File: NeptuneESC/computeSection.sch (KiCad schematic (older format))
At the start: 15 parts, among them U1 ACS712xLCTR-20A, U2 ATmega8A-AU, Y1 16MHz

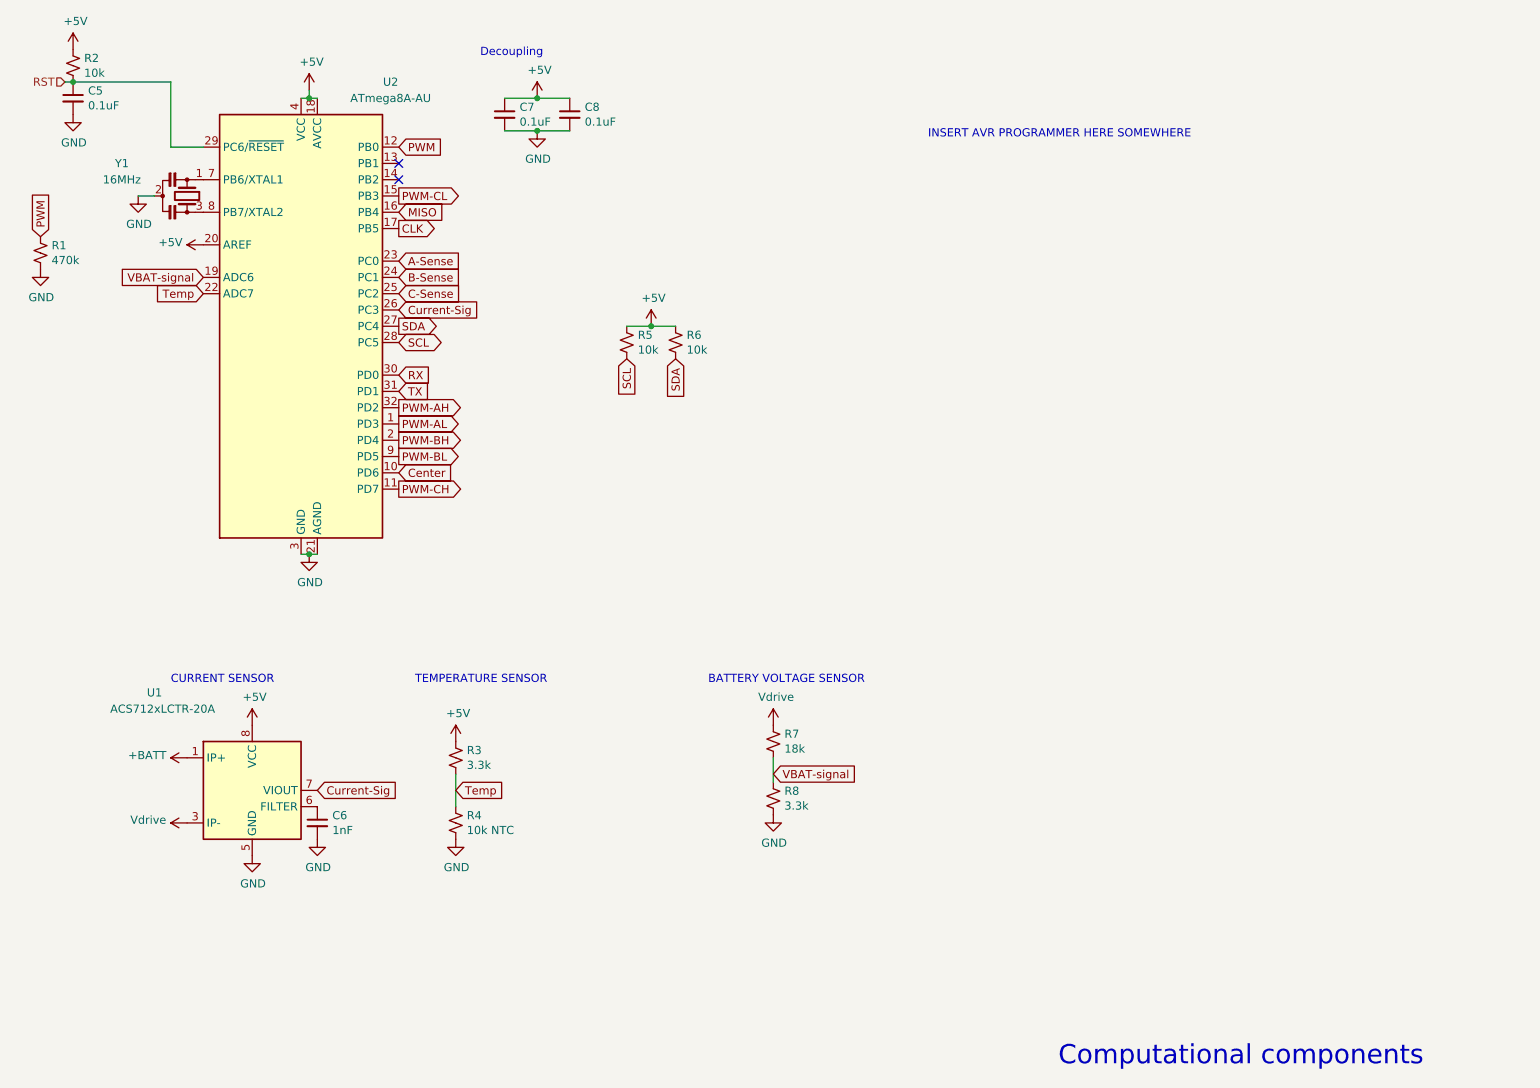
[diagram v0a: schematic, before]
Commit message: Innitial layout
Need to add motor pads
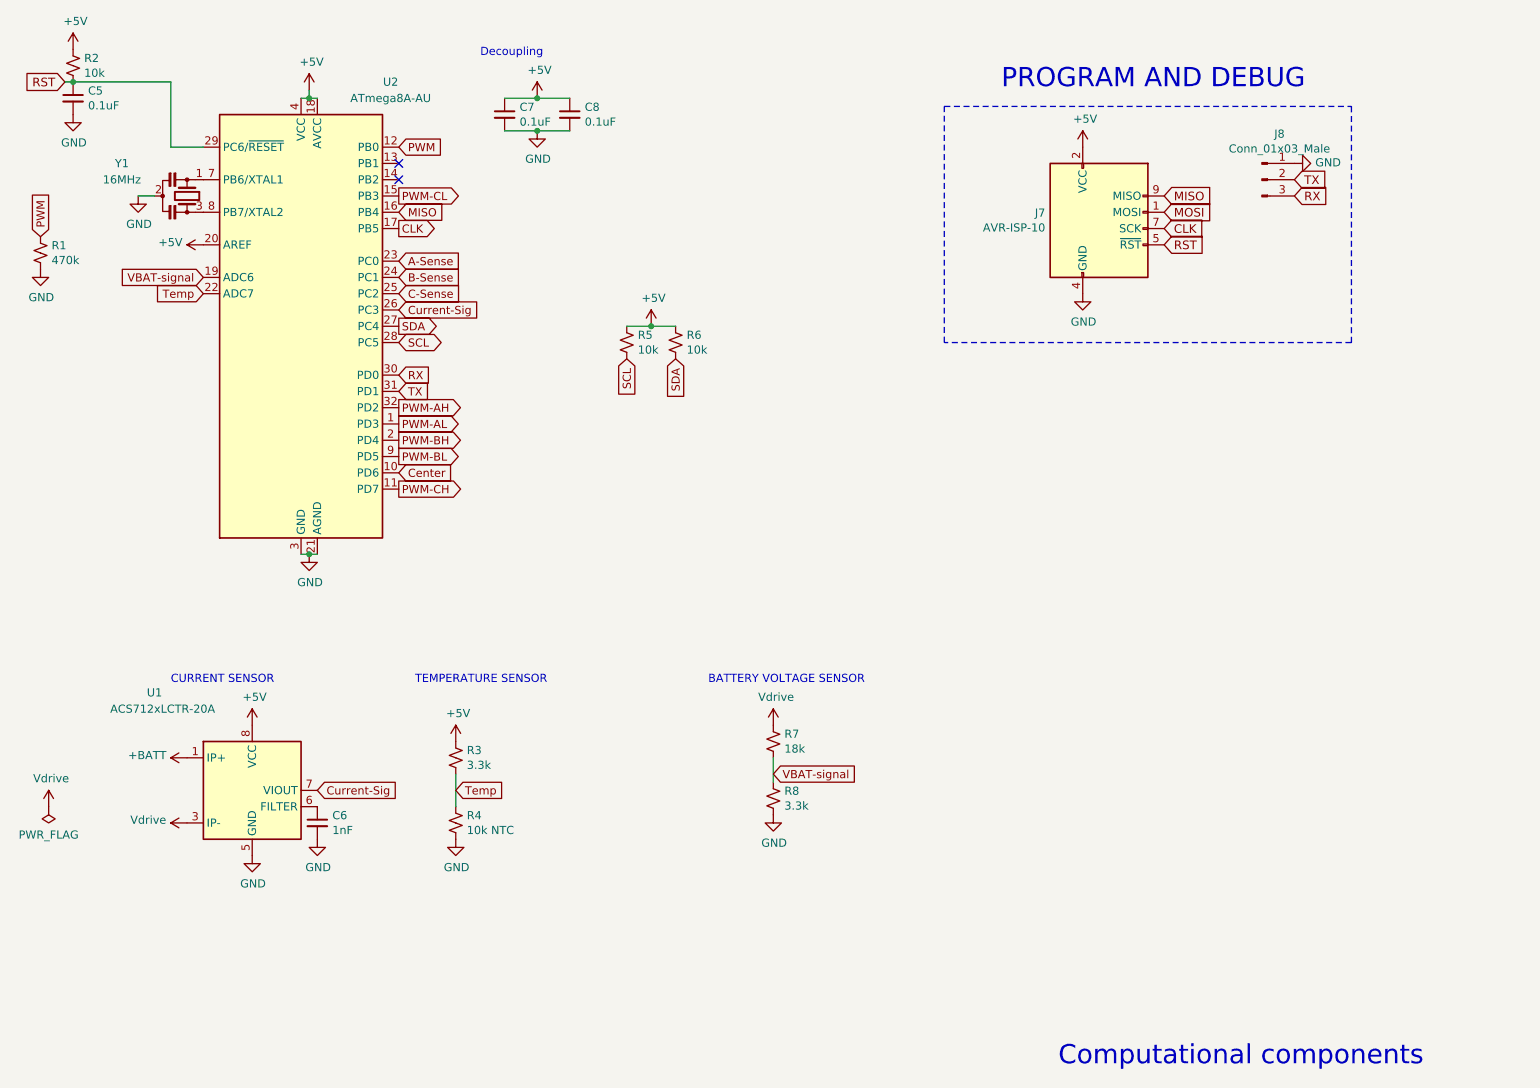
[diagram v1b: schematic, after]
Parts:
- added J7: AVR-ISP-10, Connector_IDC:IDC-Header_2x05_P2.54mm_Vertical, symbol Connector:AVR-ISP-10
- added J8: Conn_01x03_Male, Connector_PinSocket_1.27mm:PinSocket_1x03_P1.27mm_Vertical_SMD_Pin1Left, symbol Connector:Conn_01x03_Male
- C5, C6, C7, C8: footprint (none) -> Capacitor_SMD:C_0402_1005Metric
- R1, R2, R3, R4, R5, R6, R7, R8: footprint (none) -> Resistor_SMD:R_0402_1005Metric
- Y1: footprint (none) -> Used libraries:X322516MLB4SI
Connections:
- net +5V: now also J7.2 (VCC)
- net CLK: now also J7.7 (SCK)
- net GND: now also J7.10 (GND), J7.4 (GND), J7.6 (GND), J7.8 (GND), J8.1 (Pin_1)
- net MISO: now also J7.9 (MISO)
- net RST: now also J7.5 (~RST)
- net RX: now also J8.3 (Pin_3)
- net TX: now also J8.2 (Pin_2)
- new net MOSI: J7.1 (MOSI)
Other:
- note added: "PROGRAM AND DEBUG\n"
- note removed: "INSERT AVR PROGRAMMER HERE SOMEWHERE"
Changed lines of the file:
@@
 F 0 "C7" H 3792 1146 50  0000 L CNN
 F 1 "0.1uF" H 3792 1055 50  0000 L CNN
-F 2 "" H 3700 1100 50  0001 C CNN
+F 2 "Capacitor_SMD:C_0402_1005Metric" H 3700 1100 50  0001 C CNN
 F 3 "~" H 3700 1100 50  0001 C CNN
 F 4 " C1525" H 3700 1100 50  0001 C CNN "JLCPCB"
@@
 F 0 "C8" H 4192 1146 50  0000 L CNN
 F 1 "0.1uF" H 4192 1055 50  0000 L CNN
-F 2 "" H 4100 1100 50  0001 C CNN
+F 2 "Capacitor_SMD:C_0402_1005Metric" H 4100 1100 50  0001 C CNN
 F 3 "~" H 4100 1100 50  0001 C CNN
 F 4 " C1525" H 4100 1100 50  0001 C CNN "JLCPCB"
@@
 F 0 "C5" H 1142 1046 50  0000 L CNN
 F 1 "0.1uF" H 1142 955 50  0000 L CNN
-F 2 "" H 1050 1000 50  0001 C CNN
+F 2 "Capacitor_SMD:C_0402_1005Metric" H 1050 1000 50  0001 C CNN
 F 3 "~" H 1050 1000 50  0001 C CNN
 F 4 "C1525" H 1050 1000 50  0001 C CNN "JLCPCB"
@@
 F 0 "R2" H 1118 846 50  0000 L CNN
 F 1 "10k" H 1118 755 50  0000 L CNN
-F 2 "" H 1050 800 50  0001 C CNN
+F 2 "Resistor_SMD:R_0402_1005Metric" H 1050 800 50  0001 C CNN
 F 3 "~" H 1050 800 50  0001 C CNN
 F 4 "C25744" H 1050 800 50  0001 C CNN "JLCPCB"
@@
 Wire Wire Line
 	1000 900  1050 900
-Text HLabel 1000 900  0    50   Input ~ 0
-RST
 Wire Wire Line
 	1650 900  1650 1300
@@
 F 0 "Y1" V 1550 1200 50  0000 C CNN
 F 1 "16MHz" V 1650 1200 50  0000 C CNN
-F 2 "" H 1725 1600 50  0001 C CNN
+F 2 "Used libraries:X322516MLB4SI" H 1725 1600 50  0001 C CNN
 F 3 "~" H 1725 1600 50  0001 C CNN
 F 4 "C13738" V 1750 1600 50  0001 C CNN "JLCPCB"
@@
 F 0 "R1" H 918 1996 50  0000 L CNN
 F 1 "470k" H 918 1905 50  0000 L CNN
-F 2 "" H 850 1950 50  0001 C CNN
+F 2 "Resistor_SMD:R_0402_1005Metric" H 850 1950 50  0001 C CNN
 F 3 "~" H 850 1950 50  0001 C CNN
 F 4 "C25790" H 850 1950 50  0001 C CNN "JLCPCB"
@@
 	1    0    0    -1
 $EndComp
-Text Notes 6300 1250 0    50   ~ 0
-INSERT AVR PROGRAMMER HERE SOMEWHERE
 Text GLabel 4450 2600 3    50   Input ~ 0
 SCL
@@
 F 0 "R5" H 4518 2546 50  0000 L CNN
 F 1 "10k" H 4518 2455 50  0000 L CNN
-F 2 "" H 4450 2500 50  0001 C CNN
+F 2 "Resistor_SMD:R_0402_1005Metric" H 4450 2500 50  0001 C CNN
 F 3 "~" H 4450 2500 50  0001 C CNN
 F 4 "C25744" H 4450 2500 50  0001 C CNN "JLCPCB"
@@
 F 0 "R6" H 4818 2546 50  0000 L CNN
 F 1 "10k" H 4818 2455 50  0000 L CNN
-F 2 "" H 4750 2500 50  0001 C CNN
+F 2 "Resistor_SMD:R_0402_1005Metric" H 4750 2500 50  0001 C CNN
 F 3 "~" H 4750 2500 50  0001 C CNN
 F 4 "C25744" H 4750 2500 50  0001 C CNN "JLCPCB"
@@
 F 0 "C6" H 2642 5496 50  0000 L CNN
 F 1 "1nF" H 2642 5405 50  0000 L CNN
-F 2 "" H 2550 5450 50  0001 C CNN
+F 2 "Capacitor_SMD:C_0402_1005Metric" H 2550 5450 50  0001 C CNN
 F 3 "~" H 2550 5450 50  0001 C CNN
 F 4 "C1523" H 2550 5450 50  0001 C CNN "JLCPCB"
@@
 F 0 "R4" H 3468 5496 50  0000 L CNN
 F 1 "10k NTC" H 3468 5405 50  0000 L CNN
-F 2 "" H 3400 5450 50  0001 C CNN
+F 2 "Resistor_SMD:R_0402_1005Metric" H 3400 5450 50  0001 C CNN
 F 3 "~" H 3400 5450 50  0001 C CNN
 F 4 "C92371" H 3400 5450 50  0001 C CNN "JLCSMT"
@@
 F 0 "R3" H 3468 5096 50  0000 L CNN
 F 1 "3.3k" H 3468 5005 50  0000 L CNN
-F 2 "" H 3400 5050 50  0001 C CNN
+F 2 "Resistor_SMD:R_0402_1005Metric" H 3400 5050 50  0001 C CNN
 F 3 "~" H 3400 5050 50  0001 C CNN
 F 4 "C25890" H 3400 5050 50  0001 C CNN "JLCPCB"
@@
 F 0 "R7" H 5418 4996 50  0000 L CNN
 F 1 "18k" H 5418 4905 50  0000 L CNN
-F 2 "" H 5350 4950 50  0001 C CNN
+F 2 "Resistor_SMD:R_0402_1005Metric" H 5350 4950 50  0001 C CNN
 F 3 "~" H 5350 4950 50  0001 C CNN
 F 4 "C25762" H 5350 4950 50  0001 C CNN "JLCPCB"
@@
 F 0 "R8" H 5418 5346 50  0000 L CNN
 F 1 "3.3k" H 5418 5255 50  0000 L CNN
-F 2 "" H 5350 5300 50  0001 C CNN
+F 2 "Resistor_SMD:R_0402_1005Metric" H 5350 5300 50  0001 C CNN
 F 3 "~" H 5350 5300 50  0001 C CNN
 F 4 "C25890" H 5350 5300 50  0001 C CNN "JLCPCB"
@@
 Text GLabel 3050 2800 2    50   Input ~ 0
 TX
+Text GLabel 1000 900  0    53   Input ~ 0
+RST
+$Comp
+L Connector:AVR-ISP-10 J?
+U 1 1 5ED1465D
+P 7350 1800
+AR Path="/5ED1465D" Ref="J?"  Part="1"
+AR Path="/5EC82153/5ED1465D" Ref="J7"  Part="1"
+F 0 "J7" H 7020 1896 50  0000 R CNN
+F 1 "AVR-ISP-10" H 7020 1805 50  0000 R CNN
+F 2 "Connector_IDC:IDC-Header_2x05_P2.54mm_Vertical" V 7100 1850 50  0001 C CNN
+F 3 " ~" H 6075 1250 50  0001 C CNN
+	1    7350 1800
+	1    0    0    -1
+$EndComp
+$Comp
+L power:+5V #PWR?
+U 1 1 5ED14663
+P 7250 1300
+AR Path="/5ED14663" Ref="#PWR?"  Part="1"
+AR Path="/5EC82153/5ED14663" Ref="#PWR0110"  Part="1"
+F 0 "#PWR0110" H 7250 1150 50  0001 C CNN
+F 1 "+5V" H 7265 1473 50  0000 C CNN
+F 2 "" H 7250 1300 50  0001 C CNN
+F 3 "" H 7250 1300 50  0001 C CNN
+	1    7250 1300
+	1    0    0    -1
+$EndComp
+Text GLabel 7750 1600 2    53   Input ~ 0
+MISO
+Text GLabel 7750 1700 2    53   Input ~ 0
+MOSI
+Text GLabel 7750 1800 2    53   Input ~ 0
+CLK
+Text GLabel 7750 1900 2    53   Input ~ 0
+RST
+$Comp
+L power:GND #PWR?
+U 1 1 5ED1466D
+P 7250 2200
+AR Path="/5ED1466D" Ref="#PWR?"  Part="1"
+AR Path="/5EC82153/5ED1466D" Ref="#PWR0111"  Part="1"
+F 0 "#PWR0111" H 7250 1950 50  0001 C CNN
+F 1 "GND" H 7255 2027 50  0000 C CNN
+F 2 "" H 7250 2200 50  0001 C CNN
+F 3 "" H 7250 2200 50  0001 C CNN
+	1    7250 2200
+	1    0    0    -1
+$EndComp
+$Comp
+L Connector:Conn_01x03_Male J?
+U 1 1 5ED14673
+P 8350 1500
+AR Path="/5ED14673" Ref="J?"  Part="1"
+AR Path="/5EC82153/5ED14673" Ref="J8"  Part="1"
+F 0 "J8" H 8458 1781 50  0000 C CNN
+F 1 "Conn_01x03_Male" H 8458 1690 50  0000 C CNN
+F 2 "Connector_PinSocket_1.27mm:PinSocket_1x03_P1.27mm_Vertical_SMD_Pin1Left" H 8350 1500 50  0001 C CNN
+F 3 "~" H 8350 1500 50  0001 C CNN
+	1    8350 1500
+	1    0    0    -1
+$EndComp
+$Comp
+L power:GND #PWR?
+U 1 1 5ED14679
+P 8550 1400
+AR Path="/5ED14679" Ref="#PWR?"  Part="1"
+AR Path="/5EC82153/5ED14679" Ref="#PWR0112"  Part="1"
+F 0 "#PWR0112" H 8550 1150 50  0001 C CNN
+F 1 "GND" V 8555 1272 50  0000 R CNN
+F 2 "" H 8550 1400 50  0001 C CNN
+F 3 "" H 8550 1400 50  0001 C CNN
+	1    8550 1400
+	0    -1   -1   0
+$EndComp
+Text GLabel 8550 1500 2    53   Input ~ 0
+TX
+Text GLabel 8550 1600 2    53   Input ~ 0
+RX
+Text Notes 6750 950  0    118  ~ 0
+PROGRAM AND DEBUG\n
+Wire Notes Line
+	6400 1050 8900 1050
+Wire Notes Line
+	8900 1050 8900 2500
+Wire Notes Line
+	8900 2500 6400 2500
+Wire Notes Line
+	6400 2500 6400 1050
+$Comp
+L power:Vdrive #PWR0113
+U 1 1 5ED197CC
+P 900 5350
+F 0 "#PWR0113" H 700 5200 50  0001 C CNN
+F 1 "Vdrive" H 915 5523 50  0000 C CNN
+F 2 "" H 900 5350 50  0001 C CNN
+F 3 "" H 900 5350 50  0001 C CNN
+	1    900  5350
+	1    0    0    -1
+$EndComp
+$Comp
+L power:PWR_FLAG #FLG0101
+U 1 1 5ED19CE5
+P 900 5350
+F 0 "#FLG0101" H 900 5425 50  0001 C CNN
+F 1 "PWR_FLAG" H 900 5523 50  0000 C CNN
+F 2 "" H 900 5350 50  0001 C CNN
+F 3 "~" H 900 5350 50  0001 C CNN
+	1    900  5350
+	-1   0    0    1
+$EndComp
 $EndSCHEMATC
